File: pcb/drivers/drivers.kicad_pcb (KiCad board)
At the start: 2 copper layers, 51.4 x 53.3 mm, 19 parts, among them J1 Conn_01x04_Male, J2 Conn_01x04_Male, J3 Conn_01x04_Male, J4 Conn_01x04_Male, J5 Conn_01x04_Male, P1 Digital, P2 COM, P3 ADC, P4 Analog, P5 ADC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

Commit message: Polishing
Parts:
- added C2: 0.1uF, Capacitor_SMD:C_0805_2012Metric_Pad1.18x1.45mm_HandSolder, B.Cu at (108.0, 41.9)
- added C3: 0.1uF, Capacitor_SMD:C_0805_2012Metric_Pad1.18x1.45mm_HandSolder, B.Cu at (108.0, 62.9)
- added J6: Conn_01x02_Male, TerminalBlock_Phoenix:TerminalBlock_Phoenix_MKDS-1,5-2_1x02_P5.00mm_Horizontal, F.Cu at (102.9, 77.5)
- added Q5: IRLML6402, Package_TO_SOT_SMD:SOT-23, B.Cu at (95.2, 78.7)
- moved J4 5.72 mm to (95.2, 70.5)
- moved R2 4.45 mm to (96.2, 61.6)
- moved D2 4.45 mm to (108.0, 59.1)
- moved J3 3.18 mm to (102.9, 55.2)
- moved C1 2.69 mm to (87.0, 74.9), turned to 270 degrees
- moved J1 1.27 mm to (102.9, 34.3)
- moved J2 1.27 mm to (95.2, 49.5)
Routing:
- net VCC: track 52.4 -> 183.1 mm, vias 0 -> 2
- net GND: track 126.8 -> 206.0 mm, vias 0 -> 2
- net /13(SCK): track 38.4 -> 70.5 mm, vias 0 -> 2
- net Net-(J6-Pad1): track 0.00 -> 7.73 mm
- net Net-(D1-Pad9): track 33.0 -> 28.6 mm
- net /10(**/SS): track 44.0 -> 39.7 mm
- net Net-(D2-Pad6): track 5.08 -> 3.81 mm
- net Net-(D2-Pad5): track 5.08 -> 3.81 mm
- net Net-(D2-Pad4): track 5.08 -> 3.81 mm
- net Net-(D2-Pad3): track 5.08 -> 3.81 mm
- net Net-(D2-Pad14): track 5.08 -> 3.81 mm
- net Net-(D2-Pad13): track 5.08 -> 3.81 mm
- net Net-(D2-Pad12): track 5.08 -> 3.81 mm
- net Net-(D2-Pad11): track 5.08 -> 3.81 mm
- net Net-(D1-Pad6): track 5.08 -> 3.81 mm
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
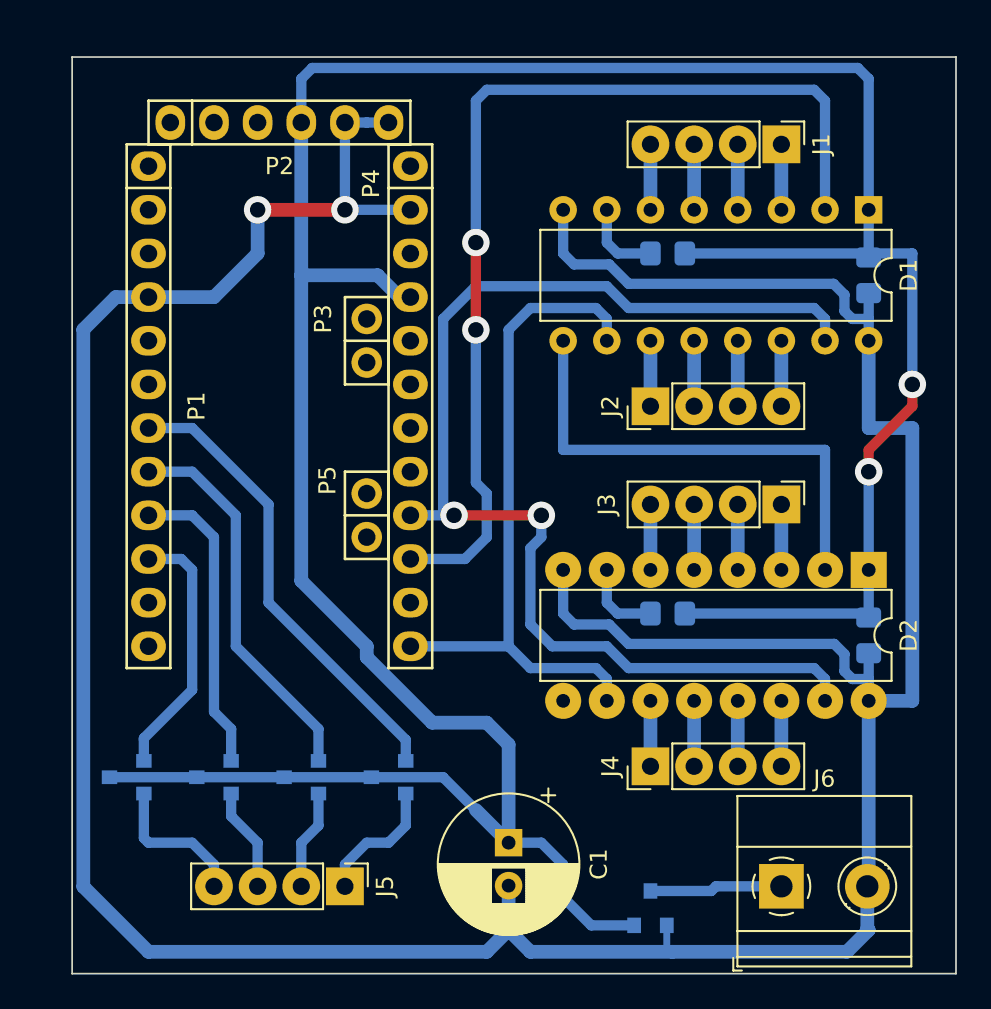
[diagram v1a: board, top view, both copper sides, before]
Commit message: Replace Arduino Pro Mini to another Arduino Pro Mini
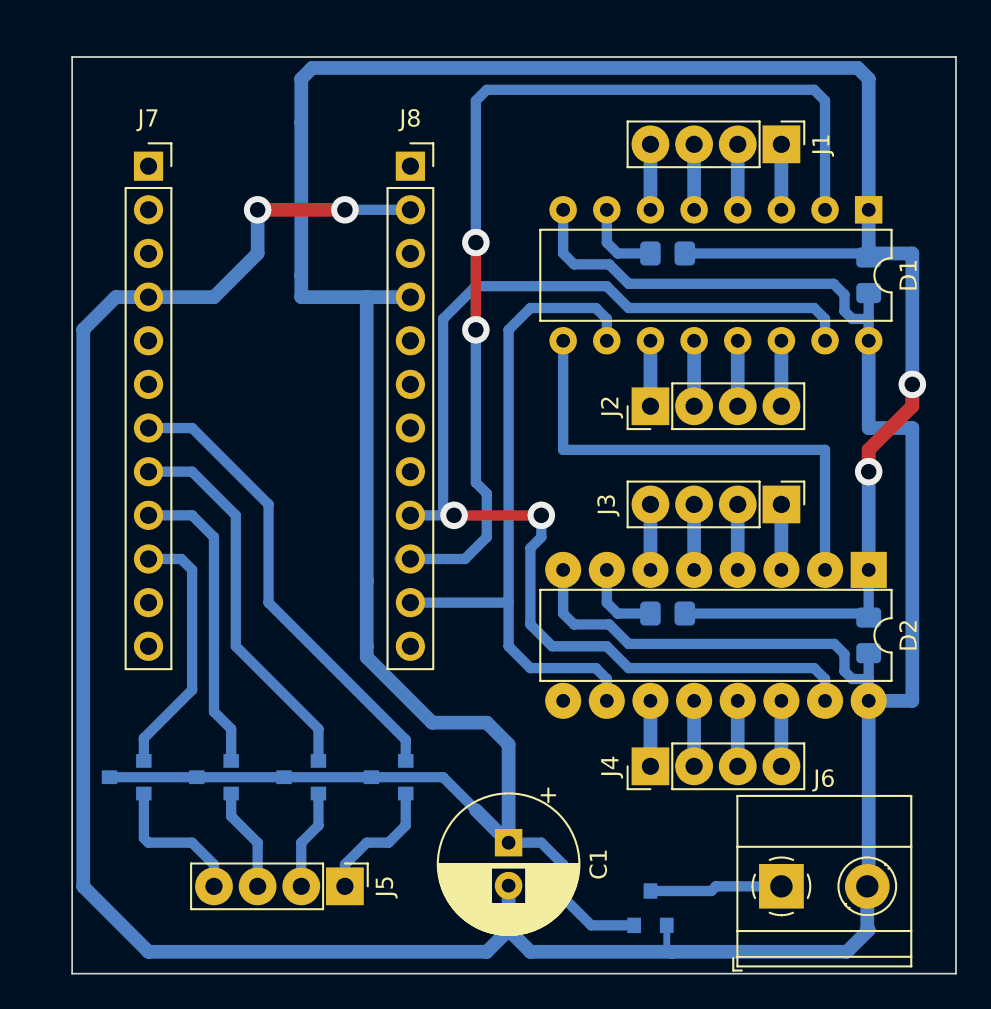
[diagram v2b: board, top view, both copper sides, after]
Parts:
- removed P1: Digital, Socket_Arduino_Pro_Mini:Socket_Strip_Arduino_1x12
- removed P2: COM, Socket_Arduino_Pro_Mini:Socket_Strip_Arduino_1x06
- removed P3, P5: ADC, Socket_Arduino_Pro_Mini:Socket_Strip_Arduino_1x02
- removed P4: Analog, Socket_Arduino_Pro_Mini:Socket_Strip_Arduino_1x12
- added J7: Conn_01x12_Female, Connector_PinSocket_2.54mm:PinSocket_1x12_P2.54mm_Vertical, F.Cu at (66.0, 35.6)
- added J8: Conn_01x12_Female, Connector_PinSocket_2.54mm:PinSocket_1x12_P2.54mm_Vertical, F.Cu at (81.3, 35.6)
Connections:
- net /10(**/SS) renamed /11
- net /13(SCK) renamed /13
- D1 pad 2: /12(MISO) -> /12
- Q2 pad 1: /5(**) -> /5
- Q3 pad 1: /6(**) -> /6
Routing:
- net /12(MISO): track 58.5 -> 0.00 mm, vias 2 -> 0
- net /12: track 0.00 -> 58.5 mm, vias 0 -> 2
- net /5(**): track 22.4 -> 0.00 mm
- net /5: track 0.00 -> 22.4 mm
- net /6(**): track 17.8 -> 0.00 mm
- net /6: track 0.00 -> 17.8 mm
- net GND: track 206.0 -> 198.4 mm
- net VCC: track 183.1 -> 180.9 mm
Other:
- board text removed: "1"

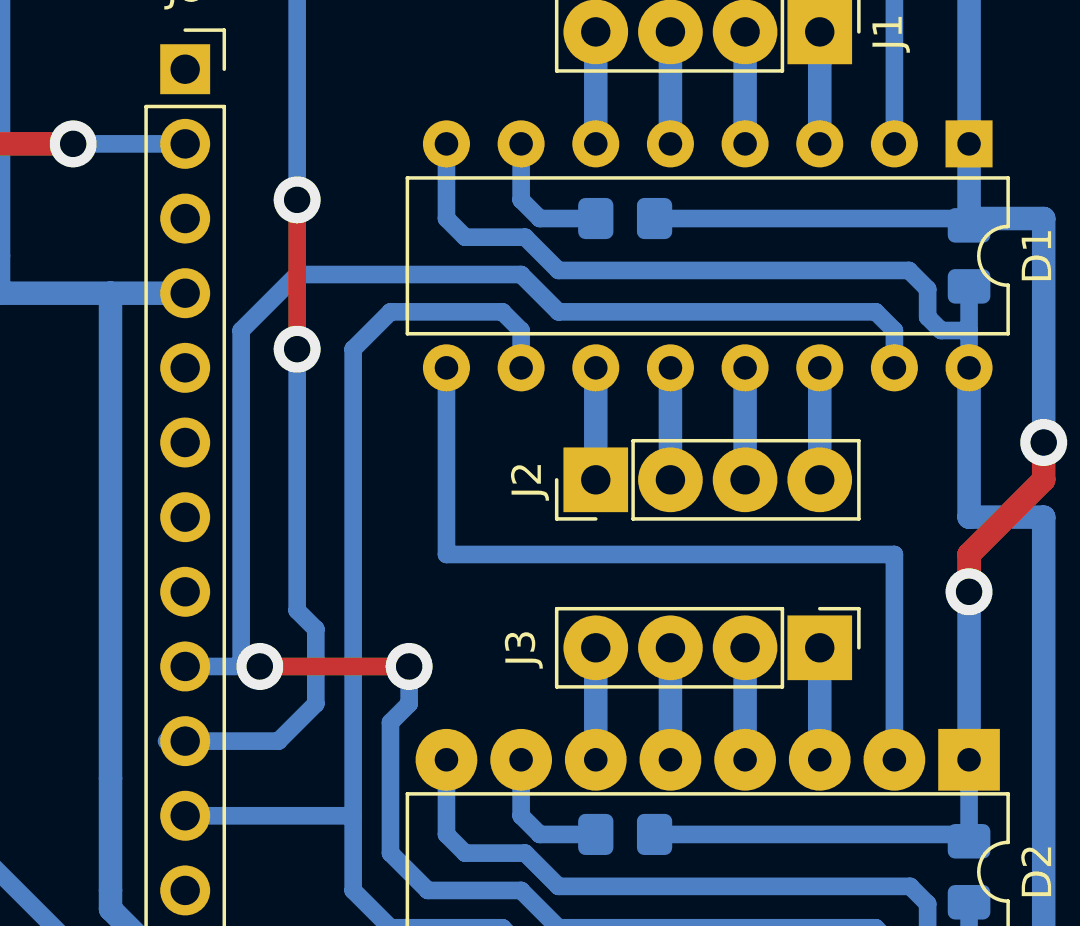
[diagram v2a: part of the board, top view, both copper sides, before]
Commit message: Swap pin 12 and 13
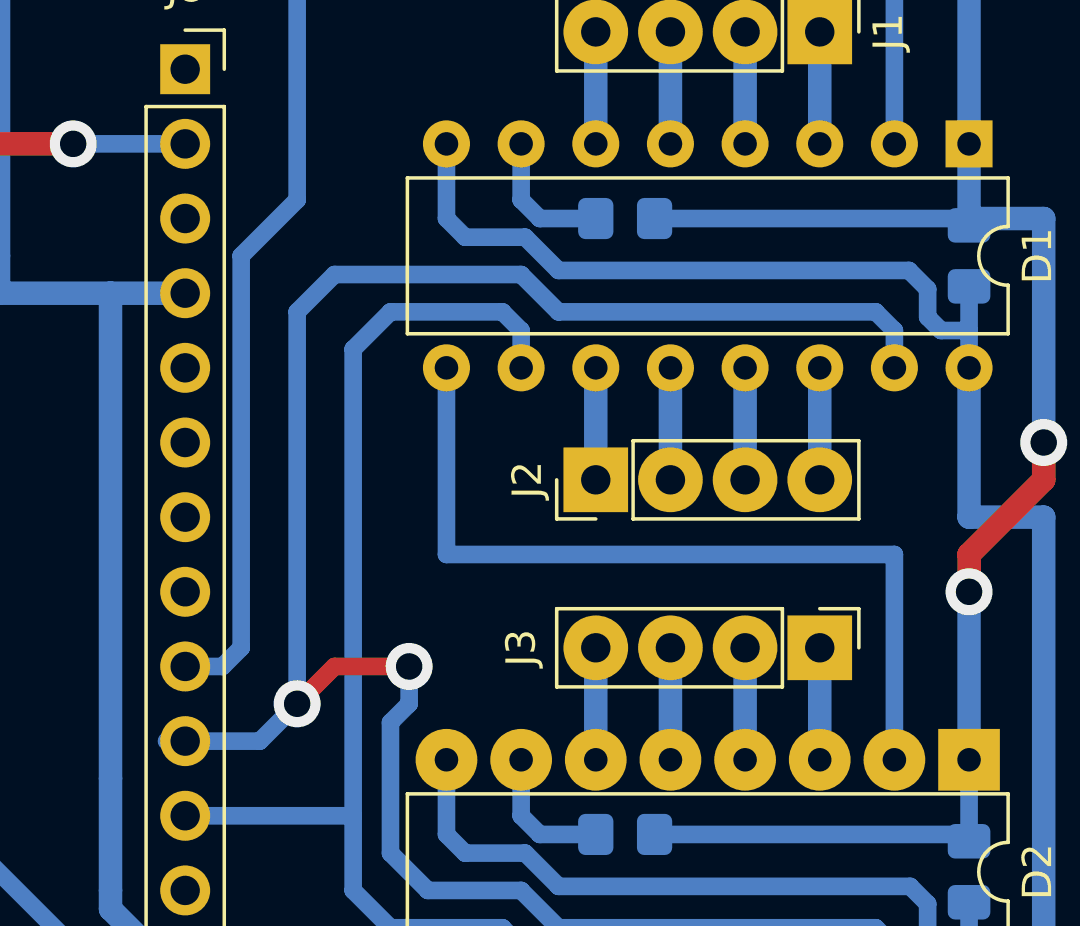
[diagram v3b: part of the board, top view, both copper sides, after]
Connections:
- D1 pad 15: /13 -> /12
- D1 pad 2: /12 -> /13
- D2 pad 15: /13 -> /12
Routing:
- net /13: track 70.5 -> 53.6 mm, vias 2 -> 0
- net /12: track 58.5 -> 71.9 mm

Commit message: Align to grid
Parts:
- moved C1 1.80 mm to (85.7, 73.7)
- moved Q1 1.80 mm to (78.7, 69.8)
- moved Q2 1.80 mm to (73.7, 69.8)
- moved J7 1.80 mm to (64.8, 34.3)
- moved J1 1.80 mm to (101.6, 33.0)
- moved J3 1.80 mm to (101.6, 54.0)
- moved J6 1.80 mm to (101.6, 76.2)
- moved Q3 1.80 mm to (68.6, 69.8)
- moved Q4 1.80 mm to (63.5, 69.8)
- moved C3 1.80 mm to (106.7, 61.6)
- moved D1 1.80 mm to (106.7, 36.8)
- moved D2 1.80 mm to (106.7, 57.8)
- moved J2 1.80 mm to (94.0, 48.3)
- moved J8 1.80 mm to (80.0, 34.3)
- moved R1 1.80 mm to (95.0, 39.4)
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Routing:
- net VCC: track 180.9 -> 179.1 mm

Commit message: Polishing
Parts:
- added H1: MountingHole, MountingHole:MountingHole_3.2mm_M3, F.Cu at (71.8, 31.8)
- added H2: MountingHole, MountingHole:MountingHole_3.2mm_M3, F.Cu at (88.9, 52.1)
- added H3: MountingHole, MountingHole:MountingHole_3.2mm_M3, F.Cu at (108.0, 31.8)
- added H4: MountingHole, MountingHole:MountingHole_3.2mm_M3, F.Cu at (64.8, 77.2)
- added H5: MountingHole, MountingHole:MountingHole_3.2mm_M3, F.Cu at (108.0, 77.2)
- moved J6 5.71 mm to (95.9, 76.2)
- moved J5 3.17 mm to (79.4, 76.2)
- moved J1 1.91 mm to (99.7, 33.0)
- moved Q5 1.91 mm to (92.1, 77.5)
- moved C1 0.64 mm to (86.4, 73.7)
- moved J3 0.64 mm to (102.2, 54.0)
- moved J7 0.64 mm to (65.4, 34.3)
- moved Q1 0.64 mm to (79.4, 69.8)
- moved Q2 0.64 mm to (74.3, 69.8)
- moved Q3 0.64 mm to (69.2, 69.8)
- moved Q4 0.64 mm to (64.1, 69.8)
- moved C2 0.63 mm to (107.3, 40.6)
- moved C3 0.63 mm to (107.3, 61.6)
- moved D1 0.63 mm to (107.3, 36.8)
- moved D2 0.63 mm to (107.3, 57.8)
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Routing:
- net VCC: track 179.1 -> 170.8 mm
- net /12: track 71.9 -> 66.7 mm
- net Net-(J6-Pad1): track 7.73 -> 3.54 mm
- net GND: track 198.4 -> 195.0 mm
- net /13: track 53.6 -> 50.3 mm
- net Net-(J5-Pad3): track 6.04 -> 8.21 mm
- net Net-(J5-Pad1): track 7.61 -> 5.81 mm
- net Net-(D1-Pad9): track 28.6 -> 27.1 mm
- net Net-(D1-Pad5): track 3.81 -> 4.86 mm
- net Net-(D1-Pad3): track 3.81 -> 4.86 mm
- net Net-(J5-Pad4): track 8.58 -> 9.63 mm
- net Net-(D1-Pad6): track 3.81 -> 4.86 mm
- net Net-(D1-Pad4): track 3.81 -> 4.86 mm
- net /11: track 39.7 -> 40.6 mm
- net /4: track 27.1 -> 27.8 mm
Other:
- board size 51.4 x 53.3 mm -> 50.8 x 53.3 mm
- board text added: "1"
- board text added: "10"
- board text added: "11"
- board text added: "12"
- board text added: "13"
- board text added: "16"
- board text added: "2"
- board text added: "3"
- board text added: "4"
- board text added: "5"
- board text added: "6"
- board text added: "7"
- board text added: "8"
- board text added: "9"
- board text added: "A0"
- board text added: "A1"
- board text added: "A2"
- board text added: "A3"
- board text added: "Arduino Pro Mini 168"
- board text added: "Gnd"
- board text added: "RX"
- board text added: "Raw"
- board text added: "TPIC6C595"
- board text added: "TX"
- board text added: "Vcc"
- board text added: "~Rst"
